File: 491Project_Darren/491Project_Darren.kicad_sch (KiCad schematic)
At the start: 43 parts, among them J1 RJ45, J2 RJ45, J3 Power Header

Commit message: renaming
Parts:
- R15, R16: value 1k -> ~
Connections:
- new net: R11., R15., R17., U4.2 (IN+)
- new net: R10., R14., R16., U4.3 (IN-)
- new net: R13., R2., R5., U3.3 (IN-)
- new net: R1., R12., R6., U3.2 (IN+)
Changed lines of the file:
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@@
 	)
 	(symbol
+		(lib_name "491_Symbols:RES_1k_805_PAN")
 		(lib_id "491_Symbols:RES_1k_805_PAN")
 		(at 198.12 118.11 0)
@@
 			)
 		)
-		(property "Value" "1k"
+		(property "Value" "~"
 			(at 203.2 120.65 0)
 			(effects
@@
 	)
 	(symbol
+		(lib_name "491_Symbols:RES_1k_805_PAN")
 		(lib_id "491_Symbols:RES_1k_805_PAN")
 		(at 198.12 128.27 0)
@@
 			)
 		)
-		(property "Value" "1k"
+		(property "Value" "~"
 			(at 203.2 130.81 0)
 			(effects

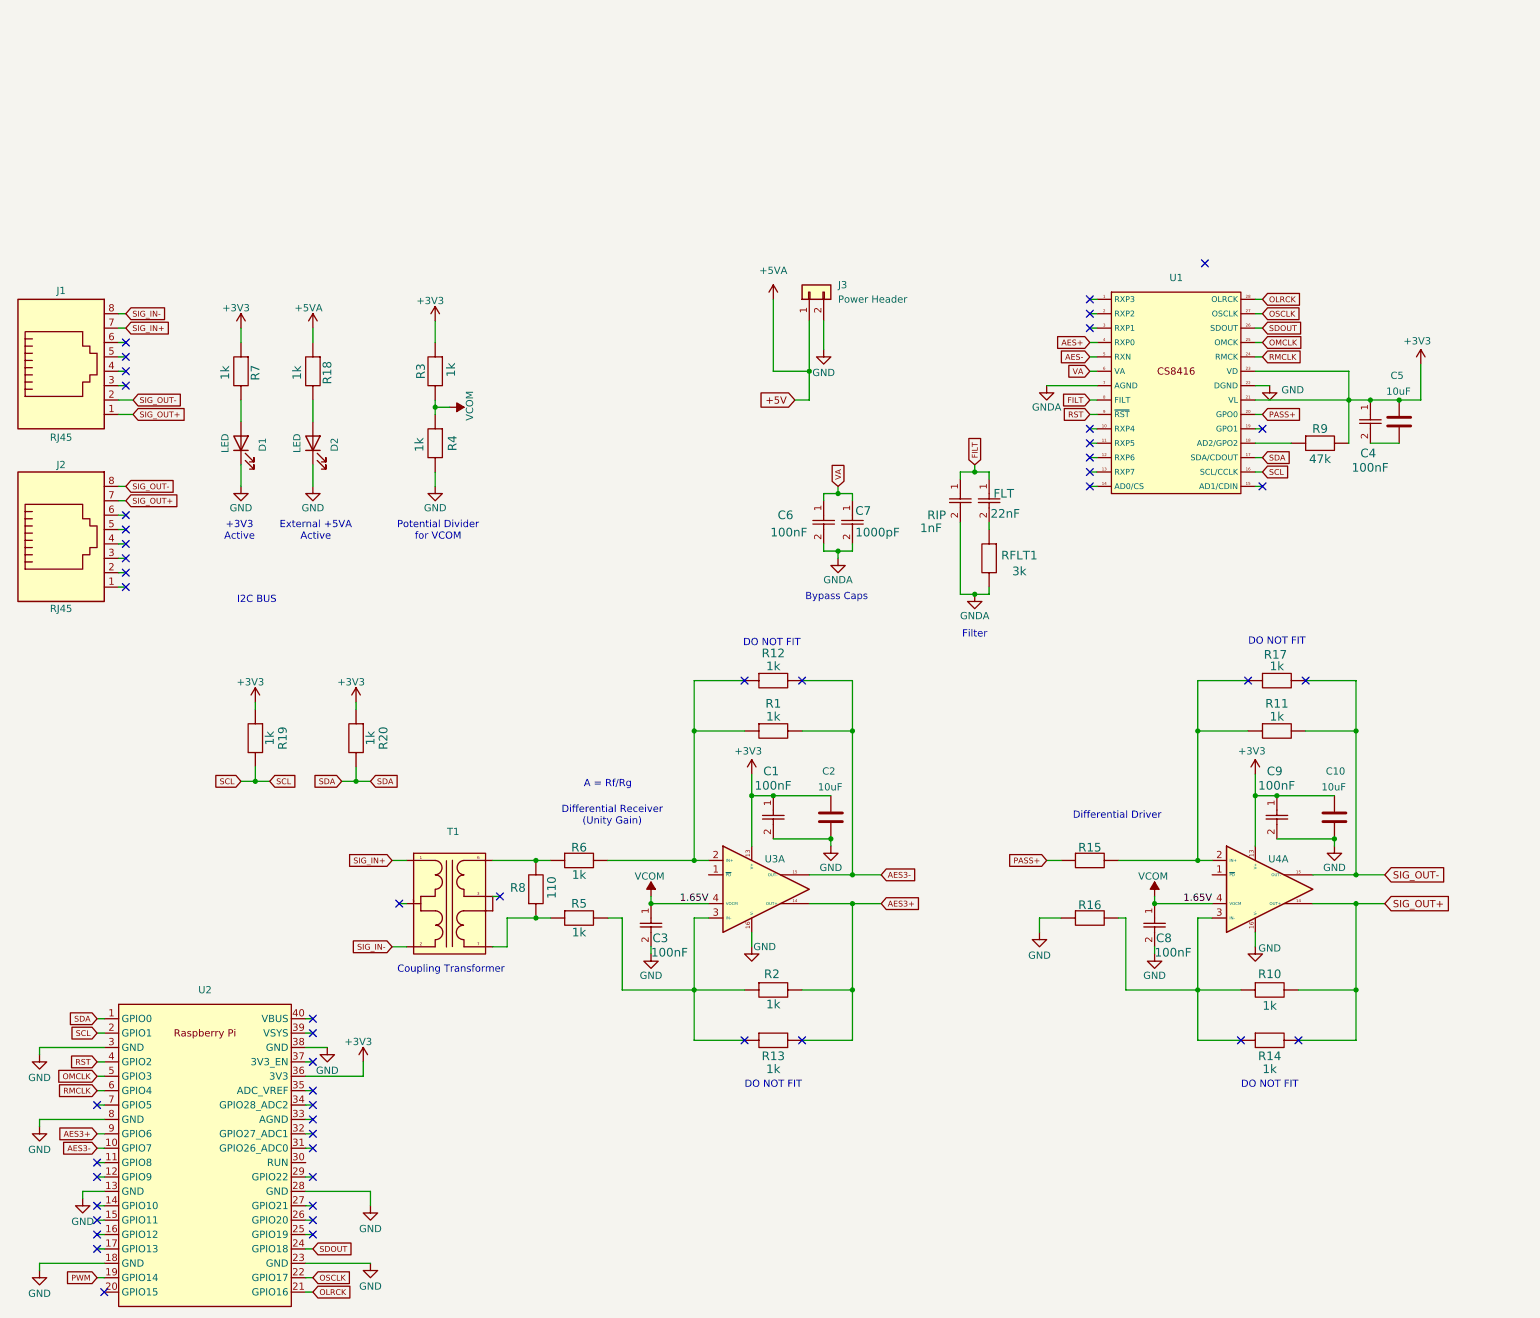
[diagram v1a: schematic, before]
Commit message: Added Test Pins
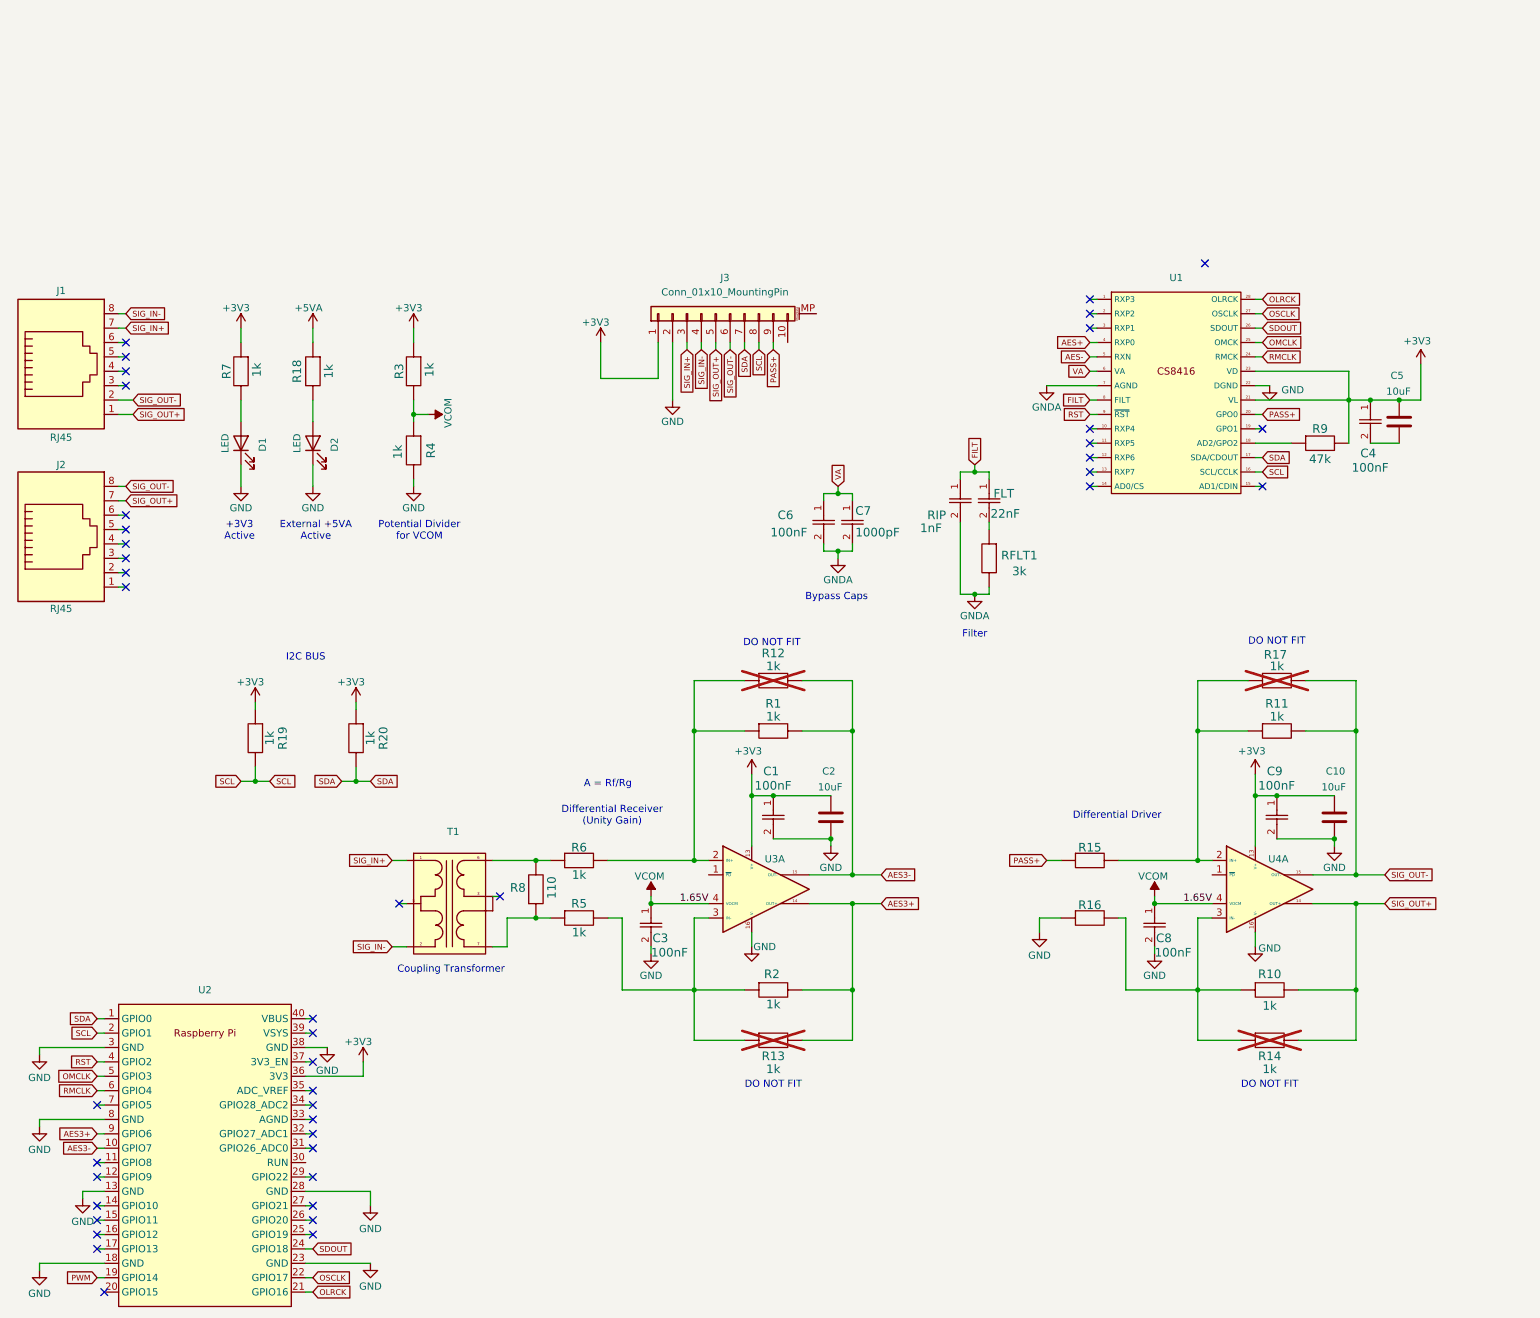
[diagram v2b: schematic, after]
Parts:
- removed J3: Power Header, symbol Connector_Generic:Conn_01x02
- added J3: Conn_01x10_MountingPin, symbol Connector_Generic_MountingPin:Conn_01x10_MountingPin
- R12, R13, R14, R17: now not fitted
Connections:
- net +3V3: now also J3.1 (Pin_1)
- net GND: now also J3.2 (Pin_2)
- net PASS+: now also J3.9 (Pin_9)
- net SCL: now also J3.8 (Pin_8)
- net SDA: now also J3.7 (Pin_7)
- net SIG_IN+: now also J3.3 (Pin_3)
- net SIG_IN-: now also J3.4 (Pin_4)
- net SIG_OUT+: now also J3.5 (Pin_5)
- net SIG_OUT-: now also J3.6 (Pin_6)
- new net: R11., R15., R17., U4.2 (IN+)
- new net: R10., R14., R16., U4.3 (IN-)
- new net: R13., R2., R5., U3.3 (IN-)
- new net: R1., R12., R6., U3.2 (IN+)
- no-connect marks 51 -> 43
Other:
- moved on the sheet: R3, R4

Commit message: PCB
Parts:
- removed C1, C4, C6, C9: 100nF, 491_Footprints:CAP_CER_100nF_SAM, symbol 491_Symbols:CAP_CER_100nF_SAM
- removed C10, C2, C5: 10uF, symbol Device:C
- removed C7: 1000pF, 491_Footprints:CAP_CER_100nF_SAM, symbol 491_Symbols:CAP_CER_100nF_SAM
- removed FLT: 22nF, 491_Footprints:CAP_CER_100nF_SAM, symbol 491_Symbols:CAP_CER_100nF_SAM
- removed R1, R10, R11, R12, R13, R14, R17, R18, R19, R2, R20, R3, R4, R5, R6, R7: 1k, 491_Footprints:RES_1k_805_PAN, symbol 491_Symbols:RES_1k_805_PAN
- removed R15, R16: ~, 491_Footprints:RES_1k_805_PAN, symbol 491_Symbols:RES_1k_805_PAN
- removed R8: 110, 491_Footprints:RES_110_805_PAN, symbol 491_Symbols:RES_110_805_PAN
- removed R9: 47k, 491_Footprints:RES_47k_805_PAN, symbol 491_Symbols:RES_47k_805_PAN
- removed RFLT1: 3k, 491_Footprints:RES_47k_805_PAN, symbol 491_Symbols:RES_47k_805_PAN
- removed RIP: 1nF, 491_Footprints:CAP_CER_100nF_SAM, symbol 491_Symbols:CAP_CER_100nF_SAM
- removed U3, U4: ~, Package_SO:TSSOP-16_4.4x5mm_P0.65mm, symbol 491_Symbols:THS4522
- added C10, C2, C9: 100nF, 491_Footprints:CAP_805_CER, symbol 491_Symbols:CAP_CER_805
- added C11, C12, C3: 10uF, 491_Footprints:CAP_ALUM, symbol 491_Symbols:CAP_ALUM
- added C4: 0.1uF, 491_Footprints:CAP_CER_0.1uF_1206, symbol 491_Symbols:CAP_CER_1206
- added C5: 1000pF, 491_Footprints:CAP_805_CER, symbol 491_Symbols:CAP_CER_805
- added C6: 1nF, 491_Footprints:CAP_805_CER, symbol 491_Symbols:CAP_CER_805
- added C7: 22nF, 491_Footprints:CAP_805_CER, symbol 491_Symbols:CAP_CER_805
- added D3: GREEN, symbol Device:LED
- added R1: 110, 491_Footprints:R_805, symbol 491_Symbols:RES_805
- added R10, R11, R12, R13, R14, R15, R17, R18, R19, R2, R20, R21, R22, R3, R4, R5, R6, R7, R8: 1k, 491_Footprints:R_805, symbol 491_Symbols:RES_805
- added R16: 47k, 491_Footprints:R_805, symbol 491_Symbols:RES_805
- added R9: 3k, 491_Footprints:R_805, symbol 491_Symbols:RES_805
- added U1: ~, Package_SO:TSSOP-16_4.4x5mm_P0.65mm, symbol 491_Symbols:THS4522
- C1: renamed from C3; footprint 491_Footprints:CAP_CER_100nF_SAM -> 491_Footprints:CAP_805_CER
- C8: footprint 491_Footprints:CAP_CER_100nF_SAM -> 491_Footprints:CAP_805_CER
- D1: value LED -> RED
- J1, J2: footprint (none) -> 491_Footprints:RJ45_Amphenol_RJHSE5380
- renumbered U1 to U3
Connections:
- net +3V3: now also C10.1, C11.1, C12.1, C2.1, C3.1, C9.1, R11.1, R15.2, R16.2, R21.2, R8.1, U1.13 (V+), U1.9 (V+)
- net +5VA: now also R10.1
- net AES3+: now also R4.2, R5.2, U1.15 (OUT-)
- net AES3-: now also R6.2, R7.2, U1.14 (OUT+)
- net FILT: now also C6.1, C7.1
- net GND: now also C11.2, C2.2, C3.2, C9.2, D3.1 (K), R12.2, R14.1, U1.12 (V-), U1.16 (V-)
- net GNDA: now also C4.2, C5.2, C6.2, R9.1
- net OLRCK: no longer U2.21 (GPIO16)
- net PASS+: now also R13.1
- net SCL: now also R15.1
- net SDA: now also R21.1
- net SIG_IN+: now also T1.2; no longer T1.1
- net SIG_IN-: now also T1.1; no longer T1.2
- net SIG_OUT+: now also R17.2, R18.2, U1.10 (OUT+)
- net SIG_OUT-: now also R19.2, R20.2, U1.11 (OUT-)
- net VA: now also C4.1, C5.1
- net VCOM: now also R11.2, R12.1, U1.4 (VOCM), U1.8 (VOCM)
- net at D1.2 (A): now also R8.2
- net at D2.2 (A): now also R10.2
- net at T1.7: now also R1.1, R3.1
- net at U3.18 (AD2/GPO2): now also R16.1
- net LED: now reaches U2.29 (GPIO22)
- net LED: now also R22.1
- net at T1.6: now also R1.2, R2.1
- new net: D3.2 (A), R22.2
- new net: R13.2, R19.1, R20.1, U1.6 (IN+)
- new net: R3.2, R6.1, R7.1, U1.3 (IN-)
- new net: R2.2, R4.1, R5.1, U1.2 (IN+)
- new net: R14.2, R17.1, R18.1, U1.7 (IN-)
- new net: C10.2, C12.2
- new net: C7.2, R9.2
- new net OLRCLK: U2.21 (GPIO16)
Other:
- note added: "Decoder"
- note added: "Differential Receiver"
- note added: "Do not populate resistors to easily modify gain of op amp"
- note added: "I2C BUS Pull-up Resistors"
- note added: "Input/Output Connectors"
- note added: "LED Indication"
- note added: "MCU"
- note added: "Raspberry Pi LED"
- note removed: "DO NOT FIT"
- note removed: "Differential Receiver (Unity Gain)"
- note removed: "I2C BUS"
- moved on the sheet: C1, C8, D1, D2, J1, J2, J3, T1, U2, U3

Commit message: Post lab
remember to keep differential pairs close together
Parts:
- removed C1, C8: 100nF, 491_Footprints:CAP_805_CER, symbol 491_Symbols:CAP_CER_100nF_SAM
- added C1, C14, C15, C16: 100nF, 491_Footprints:CAP_805_CER, symbol 491_Symbols:CAP_CER_805
- added C13, C8: 10nF, 491_Footprints:CAP_805_CER, symbol 491_Symbols:CAP_CER_805
- added R23: 50, 491_Footprints:R_805, symbol 491_Symbols:RES_805
- added R24: 52, 491_Footprints:R_805, symbol 491_Symbols:RES_805
- D1: footprint (none) -> LED_THT:LED_D3.0mm
- D2: value LED -> RED; footprint (none) -> LED_THT:LED_D3.0mm
- D3: value GREEN -> RED; footprint (none) -> LED_THT:LED_D3.0mm
- J1, J2: footprint 491_Footprints:RJ45_Amphenol_RJHSE5380 -> 491_Footprints:RJ45_Conn
- R1: value 110 -> 52
- R11: value 1k -> 100
- R12: value 1k -> 50
- R13: value 1k -> 900
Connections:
- net +5VA is gone; now on net +5V: R10.1
- net VA is gone; now on net +3V3: C4.1, C5.1, U3.6 (VA)
- net +3V3: no longer C10.1, C11.1, C12.1, C2.1, C3.1, C9.1, R11.1, R15.2, R16.2, R21.2, R8.1, U1.13 (V+), U1.9 (V+), U3.21 (VL), U3.23 (VD)
- net AES3+: now also R5.1, C8.1; no longer R5.2
- net AES3-: now also C13.1
- net GND: now also C10.2, C12.2, C1.2, C14.2, C15.2, C16.2; no longer R12.2
- net OLRCLK: now also U2.22 (GPIO17); no longer U2.21 (GPIO16)
- net OSCLK: now also U2.21 (GPIO16); no longer U2.22 (GPIO17)
- net SIG_OUT+: now also R23.2; no longer R17.2, R18.2, U1.10 (OUT+)
- net SIG_OUT-: now also R12.2; no longer R19.2, R20.2, U1.11 (OUT-)
- net at R19.1, R20.1, U1.6 (IN+): now also R11.2; no longer R13.2
- net at R3.1, T1.7: now also R24.1; no longer R1.1
- net at R2.2, R4.1, U1.2 (IN+): now also R5.2; no longer R5.1
- net at U1.1 (~{PD}): now also C14.1
- net +5V: now reaches U2.40 (VBUS)
- net +5V: now also C10.1, C11.1, C12.1, C2.1, C3.1, C9.1, R15.2, R16.2, R21.2, R8.1, U1.13 (V+), U1.9 (V+), U3.21 (VL), U3.23 (VD)
- net AES+: no longer names the net of U3.4 (RXP0)
- net AES+: now also C8.2
- net AES-: no longer names the net of U3.5 (RXN)
- net AES-: now also C13.2
- removed net VCOM: R11.2, R12.1, U1.4 (VOCM), U1.8 (VOCM)
- new net: R1.1, R24.2
- new net: R11.1, R13.2
- new net: C1.1, C16.1, U1.8 (VOCM)
- new net: C15.1, U1.4 (VOCM)
- new net: R17.2, R18.2, R23.1, U1.10 (OUT+)
- new net: R12.1, R19.2, R20.2, U1.11 (OUT-)
- no-connect marks 43 -> 40
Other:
- note added: "+5V Active"
- note added: "The twisted pair used for signal is 100ohm. Hence, 100ohm termination resistor"
- note removed: "External +5VA Active"
- note removed: "Potential Divider for VCOM"
- moved on the sheet: R13, R3

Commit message: Added Power planes, Removed dead copper?
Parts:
- removed D3: RED, LED_THT:LED_D3.0mm, symbol Device:LED
- removed R22: 1k, 491_Footprints:R_805, symbol 491_Symbols:RES_805
- J3: footprint (none) -> Connector_PinHeader_1.27mm:PinHeader_1x11_P1.27mm_Vertical
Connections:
- net +5V: now also D1.2 (A); no longer R10.1, R8.1
- net FILT: now also R9.2; no longer C7.1
- net GND: now also R10.2, R8.2; no longer D1.1 (K), D2.1 (K)
- net GNDA: now also C7.2; no longer R9.1
- net LED: now also D2.2 (A)
- net at C16.1, U1.8 (VOCM): no longer C1.1
- net at U1.5 (~{PD}): now also C1.1
- new net: D1.1 (K), R8.1
- new net: D2.1 (K), R10.1
- new net: C7.1, R9.1
- no-connect marks 40 -> 41
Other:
- note removed: "+3V3 Active"
- moved on the sheet: J3
